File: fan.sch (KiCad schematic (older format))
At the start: 4 parts

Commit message: fac pmw v1
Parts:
- added C?: CP1, Capacitor_THT:CP_Radial_D10.0mm_P2.50mm_P5.00mm, symbol Device:CP1
- added J? (x4): Conn_01x04, Connector:FanPinHeader_1x04_P2.54mm_Vertical, symbol Connector_Generic:Conn_01x04
- added Q? (x4): 2N7002, Package_TO_SOT_SMD:SOT-23, symbol Transistor_FET:2N7002
- added R? (x4): 10K, Resistor_SMD:R_0805_2012Metric, symbol Device:R
- added R? (x4): 4.7K, Resistor_SMD:R_0805_2012Metric, symbol Device:R
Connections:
- net labels added: FanSpeed02, FanSpeed03, FanSpeed04, FanSpeed05, PWM_01, PWM_02, PWM_03, PWM_04, PWM_05
- wire segments 9 -> 46

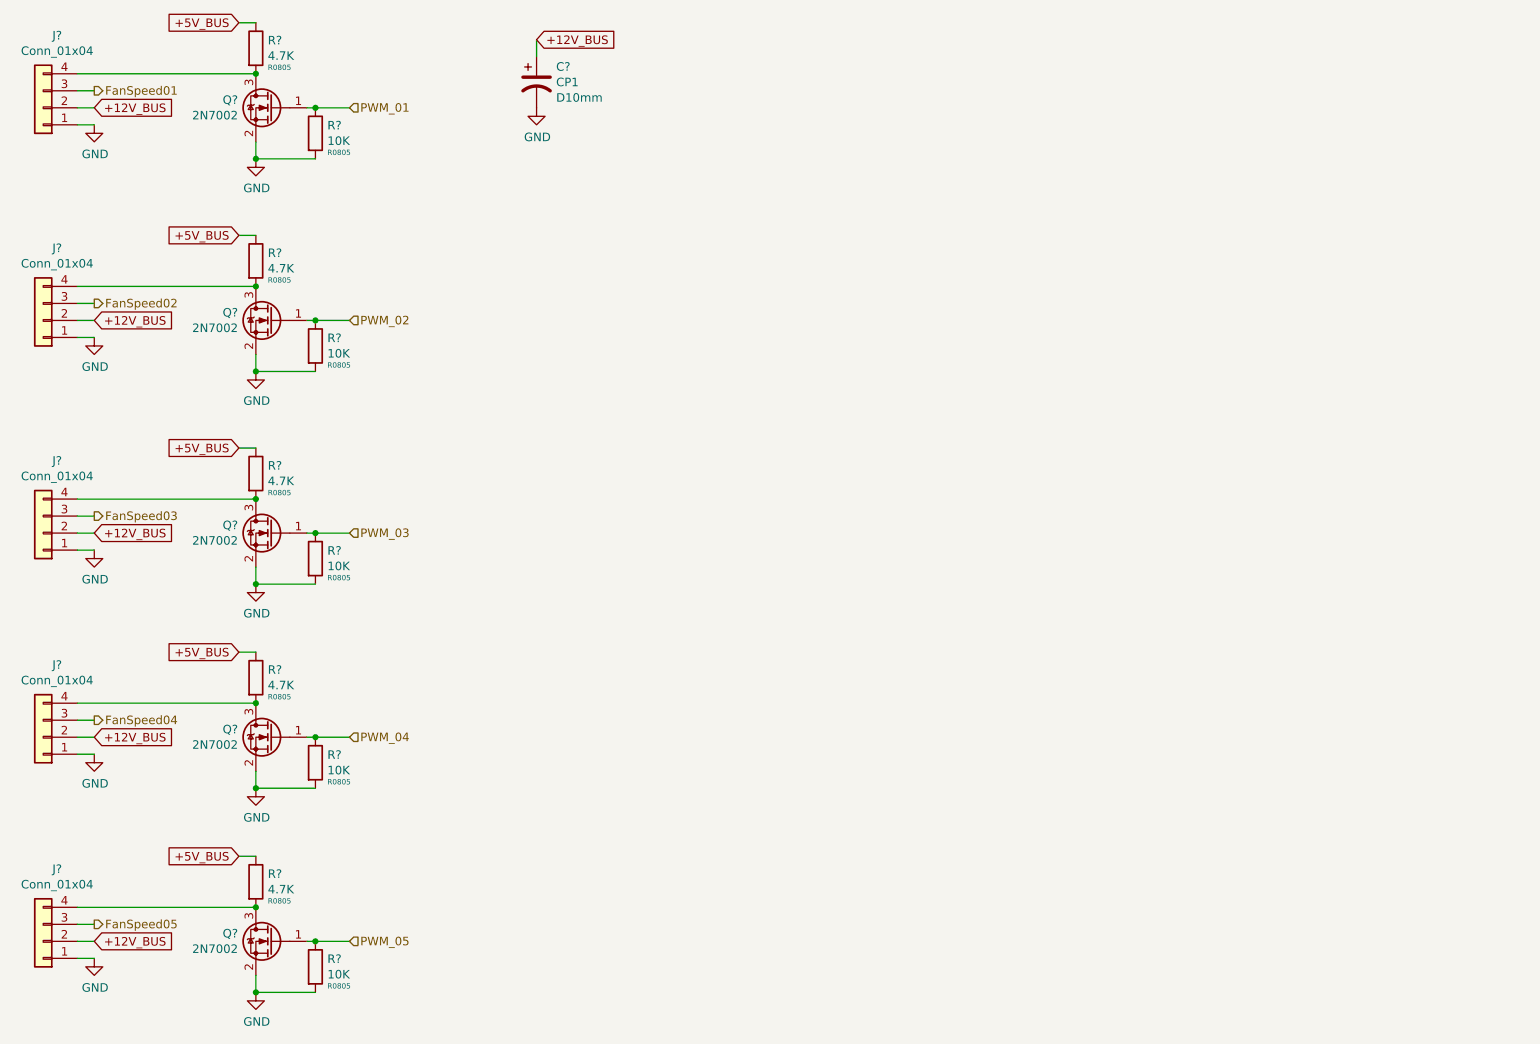
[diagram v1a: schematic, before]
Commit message: add some capacitor in fan and power_out
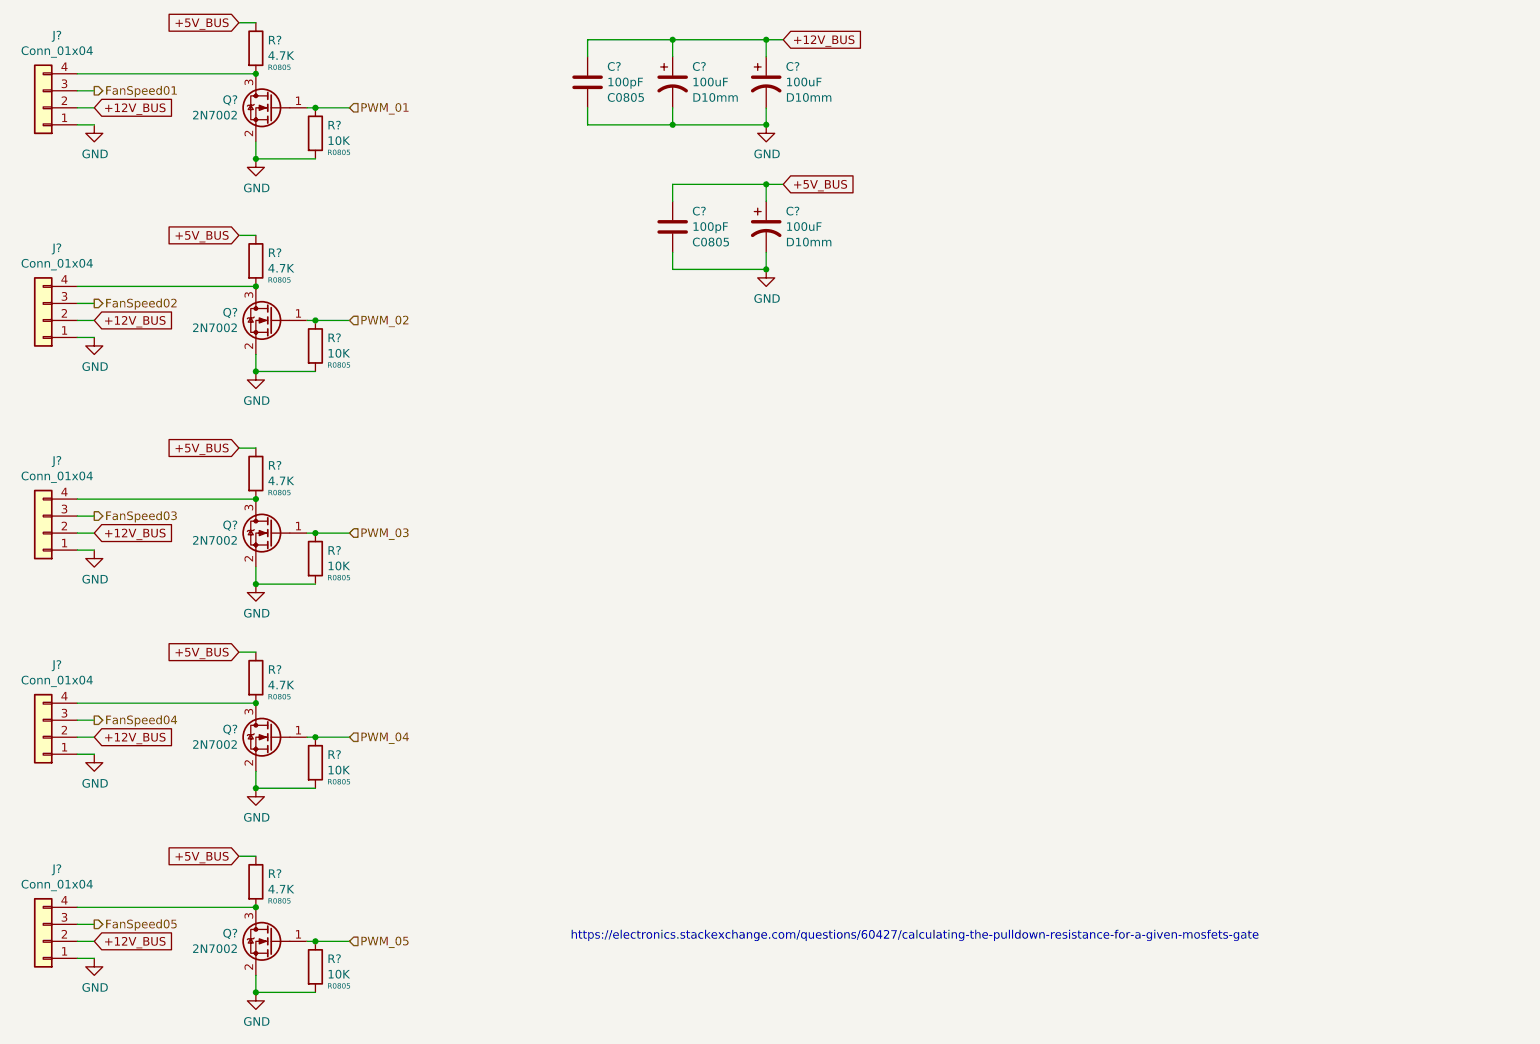
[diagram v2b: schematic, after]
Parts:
- removed C?: CP1, Capacitor_THT:CP_Radial_D10.0mm_P2.50mm_P5.00mm, symbol Device:CP1
- added C? (x3): 100uF, Capacitor_THT:CP_Radial_D10.0mm_P2.50mm_P5.00mm, symbol Device:CP1
- added C? (x2): 100pF, Capacitor_SMD:C_0805_2012Metric, symbol Device:C
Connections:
- net +12V_BUS: now also C?.1, C?.1, C?.1
- net +5V_BUS: now also C?.1, C?.1
- net GND: now also C?.2, C?.2, C?.2, C?.2, C?.2
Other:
- note added: "https://electronics.stackexchange.com/questions/60427/calculating-the-pulldown-resistance-for-a-given-mosfets-gate"
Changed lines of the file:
@@
 $Comp
 L Device:CP1 C?
-U 1 1 5E3508B7
-P 4200 1250
-F 0 "C?" H 4315 1341 50  0000 L CNN
-F 1 "CP1" H 4315 1250 50  0000 L CNN
-F 2 "Capacitor_THT:CP_Radial_D10.0mm_P2.50mm_P5.00mm" H 4315 1159 50  0001 L CNN
-F 3 "~" H 4200 1250 50  0001 C CNN
-F 4 "D10mm" H 4315 1159 50  0000 L CNN "size"
-	1    4200 1250
+U 1 1 5E360CD4
+P 5550 1250
+F 0 "C?" H 5665 1341 50  0000 L CNN
+F 1 "100uF" H 5665 1250 50  0000 L CNN
+F 2 "Capacitor_THT:CP_Radial_D10.0mm_P2.50mm_P5.00mm" H 5665 1159 50  0001 L CNN
+F 3 "~" H 5550 1250 50  0001 C CNN
+F 4 "D10mm" H 5665 1159 50  0000 L CNN "size"
+	1    5550 1250
 	1    0    0    -1
 $EndComp
-Text GLabel 4200 1000 2    50   Input ~ 0
+Text GLabel 5650 1000 2    50   Input ~ 0
 +12V_BUS
 Wire Wire Line
-	4200 1100 4200 1000
+	5550 1100 5550 1000
 $Comp
 L power:GND #PWR?
-U 1 1 5E353613
-P 4200 1400
-F 0 "#PWR?" H 4200 1150 50  0001 C CNN
-F 1 "GND" H 4205 1227 50  0000 C CNN
-F 2 "" H 4200 1400 50  0001 C CNN
-F 3 "" H 4200 1400 50  0001 C CNN
-	1    4200 1400
+U 1 1 5E360CDC
+P 5550 1500
+AR Path="/5E350920/5E360CDC" Ref="#PWR?"  Part="1"
+AR Path="/5E31859C/5E360CDC" Ref="#PWR?"  Part="1"
+F 0 "#PWR?" H 5550 1250 50  0001 C CNN
+F 1 "GND" H 5555 1327 50  0000 C CNN
+F 2 "" H 5550 1500 50  0001 C CNN
+F 3 "" H 5550 1500 50  0001 C CNN
+	1    5550 1500
 	1    0    0    -1
 $EndComp
+$Comp
+L Device:CP1 C?
+U 1 1 5E360CE3
+P 5000 1250
+F 0 "C?" H 5115 1341 50  0000 L CNN
+F 1 "100uF" H 5115 1250 50  0000 L CNN
+F 2 "Capacitor_THT:CP_Radial_D10.0mm_P2.50mm_P5.00mm" H 5115 1159 50  0001 L CNN
+F 3 "~" H 5000 1250 50  0001 C CNN
+F 4 "D10mm" H 5115 1159 50  0000 L CNN "size"
+	1    5000 1250
+	1    0    0    -1
+$EndComp
+Text GLabel 5650 1850 2    50   Input ~ 0
++5V_BUS
+$Comp
+L Device:C C?
+U 1 1 5E360CEB
+P 5000 2100
+AR Path="/5E350920/5E360CEB" Ref="C?"  Part="1"
+AR Path="/5E31859C/5E360CEB" Ref="C?"  Part="1"
+F 0 "C?" H 5115 2191 50  0000 L CNN
+F 1 "100pF" H 5115 2100 50  0000 L CNN
+F 2 "Capacitor_SMD:C_0805_2012Metric" H 5038 1950 50  0001 C CNN
+F 3 "~" H 5000 2100 50  0001 C CNN
+F 4 "C0805" H 5115 2009 50  0000 L CNN "size"
+	1    5000 2100
+	1    0    0    -1
+$EndComp
+$Comp
+L Device:CP1 C?
+U 1 1 5E360CF2
+P 5550 2100
+F 0 "C?" H 5665 2191 50  0000 L CNN
+F 1 "100uF" H 5665 2100 50  0000 L CNN
+F 2 "Capacitor_THT:CP_Radial_D10.0mm_P2.50mm_P5.00mm" H 5665 2009 50  0001 L CNN
+F 3 "~" H 5550 2100 50  0001 C CNN
+F 4 "D10mm" H 5665 2009 50  0000 L CNN "size"
+	1    5550 2100
+	1    0    0    -1
+$EndComp
+$Comp
+L power:GND #PWR?
+U 1 1 5E360CF8
+P 5550 2350
+AR Path="/5E350920/5E360CF8" Ref="#PWR?"  Part="1"
+AR Path="/5E31859C/5E360CF8" Ref="#PWR?"  Part="1"
+F 0 "#PWR?" H 5550 2100 50  0001 C CNN
+F 1 "GND" H 5555 2177 50  0000 C CNN
+F 2 "" H 5550 2350 50  0001 C CNN
+F 3 "" H 5550 2350 50  0001 C CNN
+	1    5550 2350
+	1    0    0    -1
+$EndComp
+Wire Wire Line
+	5000 1950 5000 1850
+Wire Wire Line
+	5000 1850 5550 1850
+Wire Wire Line
+	5550 1950 5550 1850
+Wire Wire Line
+	5550 1000 5000 1000
+Wire Wire Line
+	5000 1000 5000 1100
+Wire Wire Line
+	5550 1400 5550 1500
+Wire Wire Line
+	5550 1500 5000 1500
+Wire Wire Line
+	5000 1500 5000 1400
+Connection ~ 5550 1500
+Wire Wire Line
+	5550 1000 5650 1000
+Connection ~ 5550 1000
+Wire Wire Line
+	5650 1850 5550 1850
+Connection ~ 5550 1850
+Wire Wire Line
+	5550 2250 5550 2350
+Wire Wire Line
+	5000 2250 5000 2350
+Wire Wire Line
+	5000 2350 5550 2350
+Connection ~ 5550 2350
+Text Notes 4400 6300 0    50   ~ 0
+https://electronics.stackexchange.com/questions/60427/calculating-the-pulldown-resistance-for-a-given-mosfets-gate
+$Comp
+L Device:C C?
+U 1 1 5E3AF75C
+P 4500 1250
+AR Path="/5E350920/5E3AF75C" Ref="C?"  Part="1"
+AR Path="/5E31859C/5E3AF75C" Ref="C?"  Part="1"
+F 0 "C?" H 4615 1341 50  0000 L CNN
+F 1 "100pF" H 4615 1250 50  0000 L CNN
+F 2 "Capacitor_SMD:C_0805_2012Metric" H 4538 1100 50  0001 C CNN
+F 3 "~" H 4500 1250 50  0001 C CNN
+F 4 "C0805" H 4615 1159 50  0000 L CNN "size"
+	1    4500 1250
+	1    0    0    -1
+$EndComp
+Wire Wire Line
+	5000 1000 4500 1000
+Wire Wire Line
+	4500 1000 4500 1100
+Connection ~ 5000 1000
+Wire Wire Line
+	4500 1400 4500 1500
+Wire Wire Line
+	4500 1500 5000 1500
+Connection ~ 5000 1500
 $EndSCHEMATC
